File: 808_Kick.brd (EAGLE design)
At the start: 55.8 x 36.8 mm, 58 parts, among them IC1 TL072P, Q1 BC546A, Q2 BC546A, Q3 BC546A, Q4 BC546A, Q5 BC546A, Q6 BC556

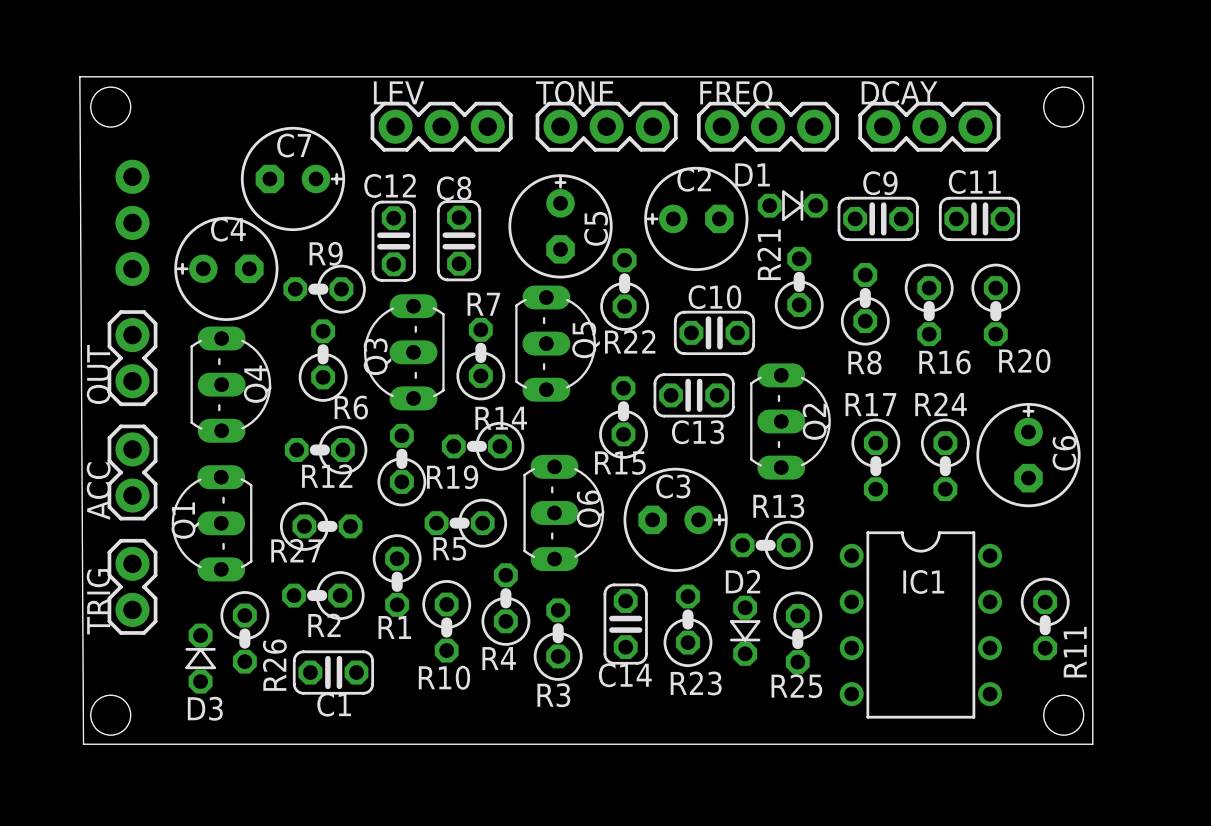
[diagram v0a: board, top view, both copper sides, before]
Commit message: Updated board
Needs all layer 25 adding to silkscreen (layer 21)
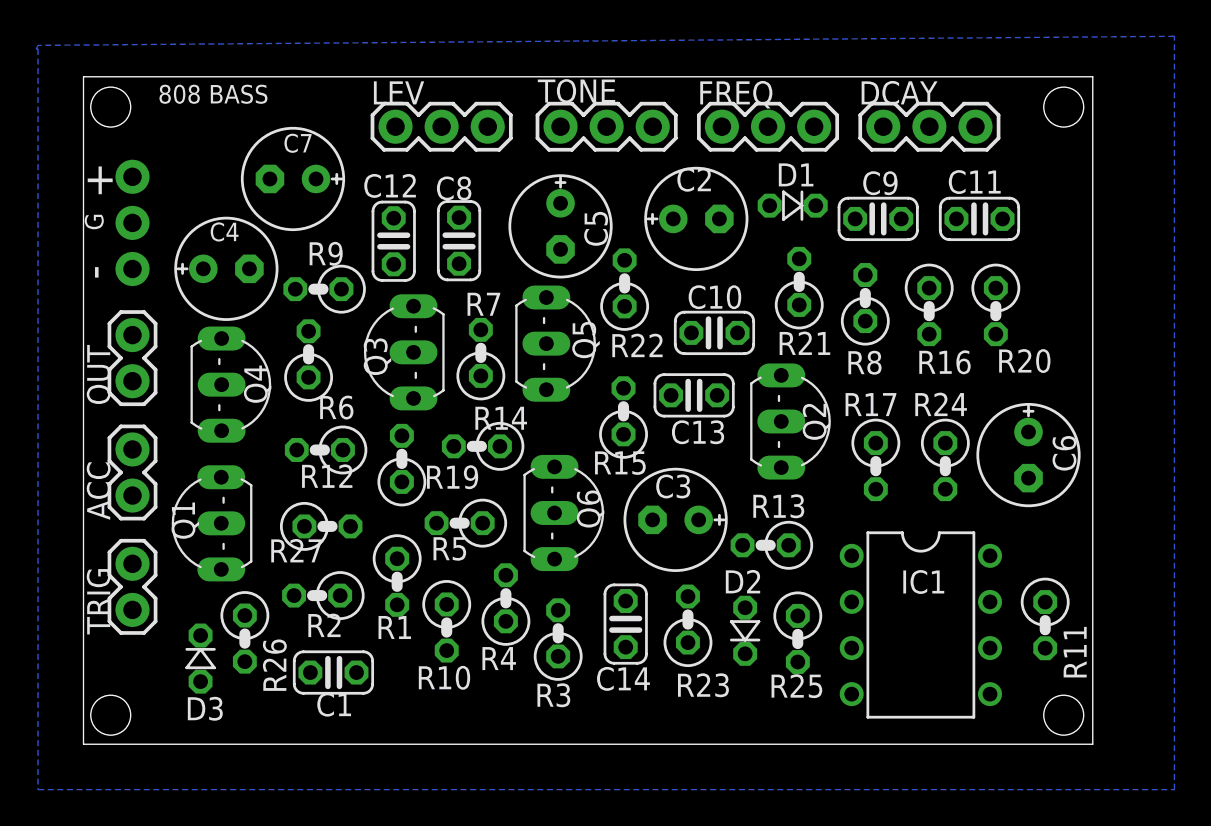
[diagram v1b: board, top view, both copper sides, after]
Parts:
- moved R6 0.80 mm to (12.4, 21.5)
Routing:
- added copper zone on layer 16, net N$5
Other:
- board size 55.8 x 36.8 mm -> 55.6 x 36.8 mm
- board text added: "+"
- board text added: "-"
- board text added: "808 BASS"
- board text added: "G"

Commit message: Updated board
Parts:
- moved R23 0.76 mm to (33.3, 6.11)
- moved C14 0.51 mm to (29.9, 6.11)
- moved R25 0.31 mm to (39.4, 6.11)
- moved D2 0.14 mm to (36.5, 6.11)
